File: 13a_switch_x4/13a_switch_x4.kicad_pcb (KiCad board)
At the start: 2 copper layers, 19.7 x 38.1 mm, 21 parts, among them P1 CONN_01X01, P2 CONN_01X01, P3 CONN_01X05, P4 CONN_01X01, P5 CONN_01X01, P6 CONN_01X01, P7 CONN_01X01, P8 CONN_01X01, Q1 Q_NMOS_GDSD, Q2 Q_NMOS_GDSD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

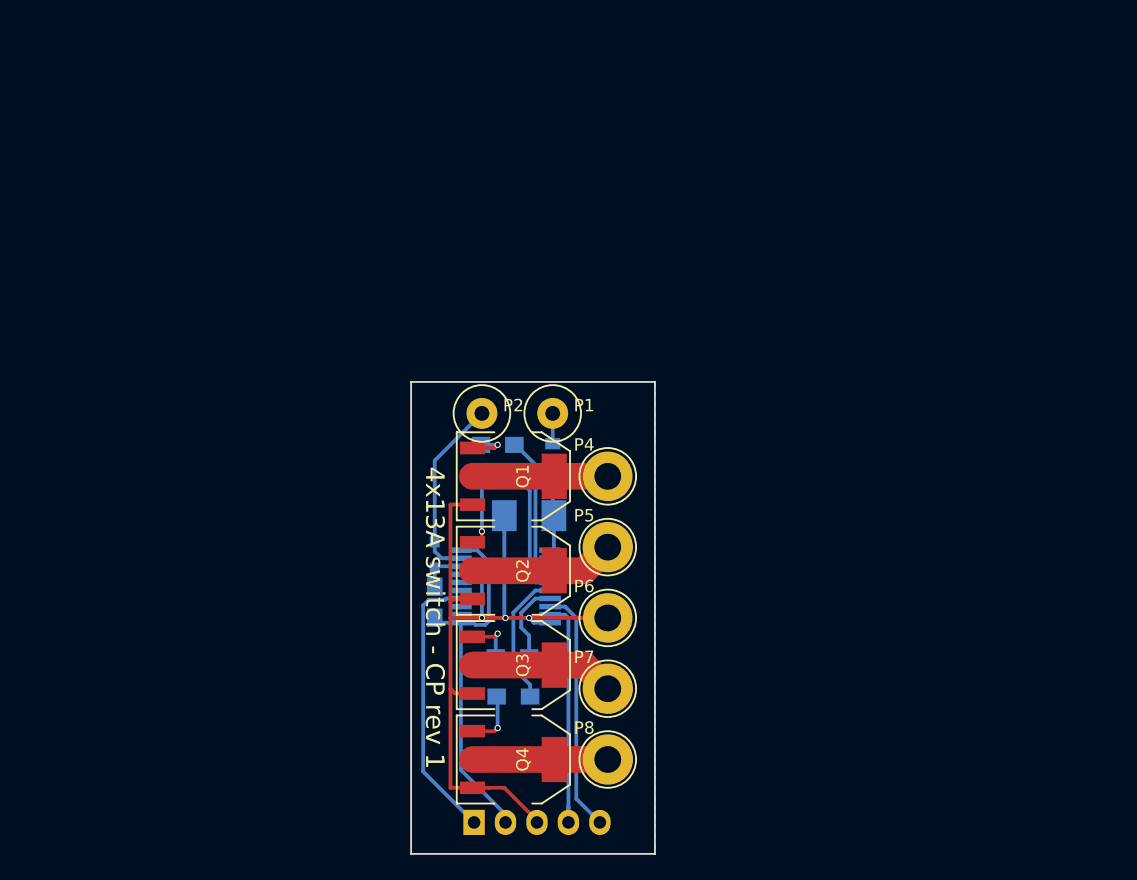
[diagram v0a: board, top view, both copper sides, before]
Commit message: 13a_switch rev2
- daisy-chain connector
- adding a DIP switch to select the LIN device
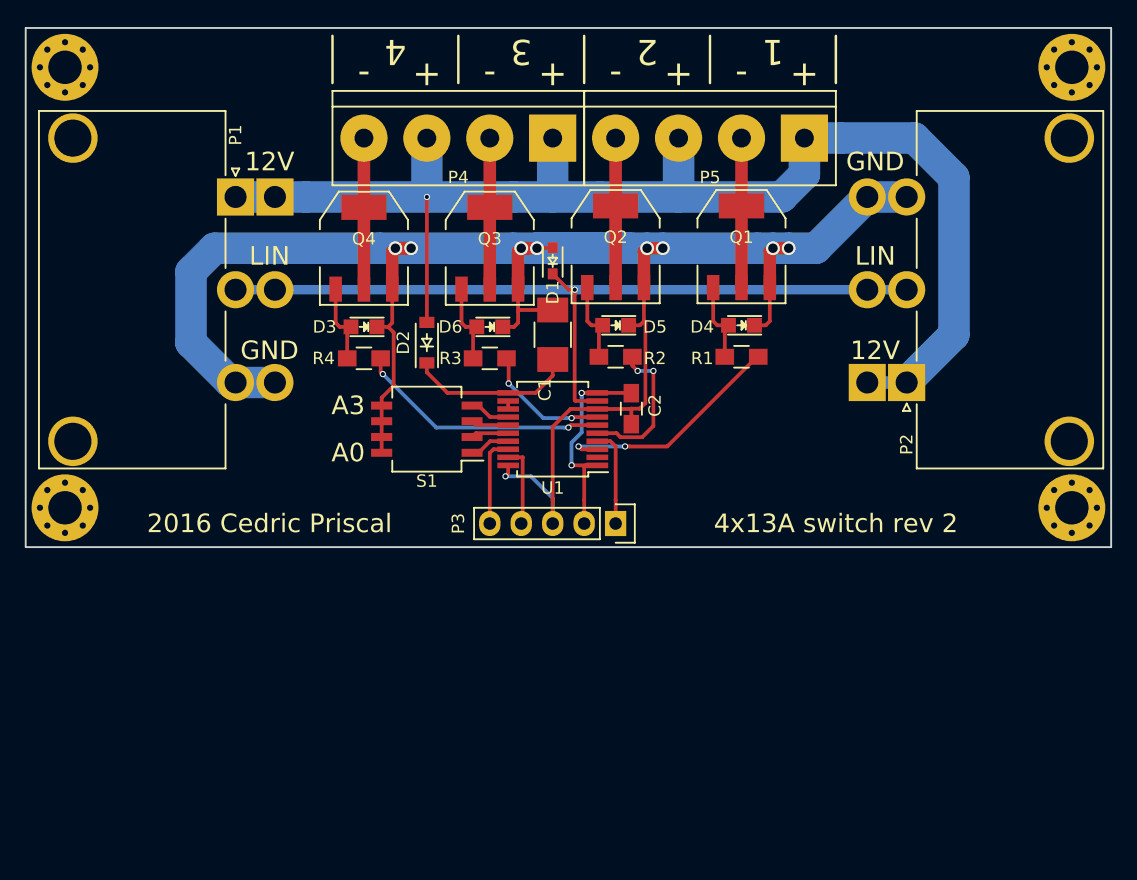
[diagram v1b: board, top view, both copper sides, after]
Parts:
- removed P6, P7, P8: CONN_01X01, Connect:1pin
- added D3: LITEON-LTST-C170KGKT, LEDs:LED_0805, F.Cu at (131.4, 73.0)
- added D4: LITEON-LTST-C170KGKT, LEDs:LED_0805, F.Cu at (161.9, 72.9)
- added D5: LITEON-LTST-C170KGKT, LEDs:LED_0805, F.Cu at (151.8, 72.9)
- added D6: LITEON-LTST-C170KGKT, LEDs:LED_0805, F.Cu at (141.6, 73.0)
- added REF**: MountingHole_2.7mm_Pad_Via, Mounting_Holes:MountingHole_2.7mm_Pad_Via, F.Cu at (188.6, 87.6)
- added REF**: MountingHole_2.7mm_Pad_Via, Mounting_Holes:MountingHole_2.7mm_Pad_Via, F.Cu at (107.3, 87.6)
- added REF**: MountingHole_2.7mm_Pad_Via, Mounting_Holes:MountingHole_2.7mm_Pad_Via, F.Cu at (188.6, 52.1)
- added REF**: MountingHole_2.7mm_Pad_Via, Mounting_Holes:MountingHole_2.7mm_Pad_Via, F.Cu at (107.3, 52.1)
- added S1: DIP_SWITCH_4, footprints:Copal_CHS-04TB, F.Cu at (136.5, 81.3)
- C1, C2, D1, D2, U1: moved to F.Cu
- P1, P2: value CONN_01X01 -> MOLEX-0431603103; footprint Connect:1pin -> Connectors_Molex:Molex_Sabre_43160-XX03_03x7.49mm_Angled_BoardLock
- P3: value CONN_01X05 -> MOLEX-22-28-6050; moved to F.Cu
- P4, P5: value CONN_01X01 -> TE-282836-4; footprint Connect:1pin -> Connect:bornier4
- R1, R2, R3, R4: value 1K -> 150; moved to F.Cu
- moved Q4 43.0 mm to (131.4, 66.7), turned to 0 degrees
- moved P2 34.4 mm to (175.3, 77.5), turned to 90 degrees
- moved P5 34.0 mm to (159.4, 57.8), turned to 180 degrees
- moved Q3 33.7 mm to (141.6, 66.7), turned to 0 degrees
- moved P1 31.0 mm to (121.1, 62.5), turned to 270 degrees
- moved P4 29.9 mm to (139.1, 57.8), turned to 180 degrees
- moved R4 29.9 mm to (131.4, 75.6)
- moved Q2 27.4 mm to (151.8, 66.5), turned to 0 degrees
- moved P3 26.7 mm to (151.8, 88.9)
- moved Q1 26.1 mm to (161.9, 66.5), turned to 0 degrees
- moved D1 25.6 mm to (146.7, 67.7), turned to 90 degrees
- moved R3 24.2 mm to (141.6, 75.6)
- moved C2 22.3 mm to (153.0, 79.6), turned to 270 degrees
- moved R1 20.9 mm to (161.9, 75.4)
- moved C1 14.7 mm to (146.7, 73.7), turned to 90 degrees
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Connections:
- D2 pad 2: Net-(D2-Pad2) -> /12V_UNPROTECTED
- P1 pad 1: Net-(D2-Pad2) -> /12V_UNPROTECTED
- P2 pad 1: /LBUS -> /12V_UNPROTECTED
- P4 pad 1: /OUT_1 -> /12V_UNPROTECTED
- P5 pad 1: /OUT_2 -> /12V_UNPROTECTED
- R1 pad 2: Net-(R1-Pad2) -> /CMD_1
- R2 pad 2: Net-(R2-Pad2) -> /CMD_2
- R3 pad 2: Net-(R3-Pad2) -> /CMD_3
- R4 pad 2: Net-(R4-Pad2) -> /CMD_4
- U1 pad 14: Net-(R1-Pad2) -> /A3
- U1 pad 15: Net-(R2-Pad2) -> /A2
- U1 pad 16: Net-(R4-Pad2) -> /A1
- U1 pad 17: Net-(R3-Pad2) -> /A0
- U1 pad 3: (no net) -> /CMD_1
- U1 pad 5: (no net) -> /CMD_2
- U1 pad 6: (no net) -> /CMD_4
- U1 pad 7: (no net) -> /CMD_3
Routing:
- net /12V_UNPROTECTED: track 0.00 -> 123.3 mm, vias 0 -> 1
- net GND: track 69.7 -> 166.2 mm, vias 3 -> 9
- net /LBUS: track 15.1 -> 67.2 mm, vias 0 -> 1
- net /CMD_4: track 0.00 -> 20.5 mm, vias 0 -> 2
- net /CMD_1: track 0.00 -> 19.1 mm, vias 0 -> 2
- net //MCLR: track 22.5 -> 7.88 mm
- net Net-(R1-Pad2): track 12.4 -> 0.00 mm
- net /CMD_2: track 0.00 -> 12.1 mm, vias 0 -> 2
- net /ICSPCLK: track 19.3 -> 7.30 mm
- net +5V: track 29.8 -> 18.0 mm, vias 0 -> 2
- net /ICSPDAT: track 18.2 -> 6.57 mm
- net Net-(R4-Pad2): track 11.0 -> 0.00 mm
- net Net-(R2-Pad2): track 10.5 -> 0.00 mm
- net /CMD_3: track 0.00 -> 10.5 mm, vias 0 -> 2
- net +12V: track 5.44 -> 13.5 mm
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- removed copper zone on F.Cu, net GND
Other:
- board size 19.7 x 38.1 mm -> 87.6 x 41.9 mm
- board text added: "+"
- board text added: "-"
- board text added: "1"
- board text added: "2"
- board text added: "2016 Cedric Priscal"
- board text added: "3"
- board text added: "4"
- board text added: "4x13A switch rev 2"
- board text added: "A0"
- board text added: "A3"
- board text removed: "4x13A switch - CP rev 1"
